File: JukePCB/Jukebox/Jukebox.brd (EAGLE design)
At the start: 133.5 x 197 mm, 31 parts, among them CN1 1X4-BIG

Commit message: board proto 1
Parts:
- moved A2 12.0 mm to (-15.0, 14.0)
- moved N1 12.0 mm to (-15.0, 26.0)
- moved CONTROL1 6.00 mm to (-30.7, -26.0)
- moved CN1 2.00 mm to (-38.3, 48.0)
- moved CONTROL2 1.00 mm to (-30.7, -29.0)
- moved J2 0.70 mm to (-35.8, 54.0)
- turned AUXIN to 90 degrees
- turned AUXOUT to 90 degrees
- turned FROMNEEDLE to 90 degrees
- turned TOAMP to 90 degrees
- turned TOLIGHT to 90 degrees
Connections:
- net GND: now also U$1.GND1
- net N$31: now also U$1.A7; no longer U$1.A3
- net N$32: now also J4.1
- net N$36: now also U$1.A3; no longer U$1.A7
- net N$8: no longer J4.1
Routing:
- net GND: track 0.00 -> 447.8 mm, vias 0 -> 8
- net N$4: track 0.00 -> 402.2 mm, vias 0 -> 2
- net N$3: track 0.00 -> 383.3 mm, vias 0 -> 4
- net N$2: track 0.00 -> 364.3 mm, vias 0 -> 4
- net N$1: track 0.00 -> 358.2 mm, vias 0 -> 4
- net N$10: track 0.00 -> 355.0 mm, vias 0 -> 2
- net N$11: track 0.00 -> 274.1 mm
- net N$27: track 0.00 -> 214.7 mm, vias 0 -> 4
- net N$32: track 0.00 -> 199.8 mm, vias 0 -> 2
- net N$8: track 0.00 -> 150.3 mm
- net N$5: track 0.00 -> 144.5 mm
- net N$6: track 0.00 -> 138.8 mm
- net N$7: track 0.00 -> 133.1 mm
- net N$22: track 0.00 -> 129.1 mm, vias 0 -> 4
- net N$37: track 0.00 -> 126.8 mm, vias 0 -> 2
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
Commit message: almost final routes
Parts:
- A1, A2, N1, N2: value 10k -> 1k
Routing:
- net GND: track 447.8 -> 113.8 mm, vias 8 -> 0
- net N$34: track 118.2 -> 120.8 mm
- net N$25: track 126.3 -> 128.1 mm
- net N$37: track 126.8 -> 128.2 mm
- net N$22: track 129.1 -> 130.2 mm
- added copper zone on layer 16, net GND

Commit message: Anime.mp4
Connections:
- net GND: now also U$8.12; no longer U$8.1
- net N$8: now also U$8.10; no longer U$8.3
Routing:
- net GND: track 113.8 -> 0.00 mm
- net N$8: track 150.3 -> 121.0 mm
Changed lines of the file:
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@@
 </signal>
 <signal name="N$8">
-<contactref element="U$8" pad="3"/>
 <contactref element="U$14" pad="3"/>
-<wire x1="29" y1="-86" x2="34.5" y2="-86" width="1.4224" layer="16"/>
-<wire x1="34.5" y1="-86" x2="34.5" y2="-96.5" width="1.4224" layer="16"/>
-<wire x1="34.5" y1="-96.5" x2="65" y2="-96.5" width="1.4224" layer="16"/>
-<wire x1="65" y1="-96.5" x2="65" y2="2.5" width="1.4224" layer="16"/>
-<wire x1="65" y1="2.5" x2="60.25" y2="2.25" width="1.4224" layer="16"/>
+<contactref element="U$8" pad="10"/>
+<wire x1="29" y1="-86" x2="34.75" y2="-86" width="1.4224" layer="16"/>
+<wire x1="34.75" y1="-86" x2="34.75" y2="-95.75" width="1.4224" layer="16"/>
+<wire x1="34.75" y1="-95.75" x2="65.25" y2="-95.75" width="1.4224" layer="16"/>
+<wire x1="65.25" y1="-95.75" x2="65.25" y2="-26" width="1.4224" layer="16"/>
+<wire x1="65.25" y1="-26" x2="60.25" y2="-26" width="1.4224" layer="16"/>
+<wire x1="60.25" y1="-26" x2="60.25" y2="-25.75" width="1.4224" layer="16"/>
 </signal>
 <signal name="N$33">
@@
 <contactref element="TOLIGHT" pad="1"/>
 <contactref element="U$7" pad="6"/>
-<contactref element="U$8" pad="1"/>
 <contactref element="J3" pad="1"/>
 <contactref element="U$13" pad="1"/>
@@
 <contactref element="U$1" pad="GND"/>
 <contactref element="CONTROL2" pad="1"/>
-<wire x1="-37" y1="-10" x2="-37" y2="2" width="0.4064" layer="16"/>
-<wire x1="-37" y1="2" x2="-37" y2="14" width="0.4064" layer="16"/>
-<wire x1="-37" y1="14" x2="-37" y2="26" width="0.4064" layer="16"/>
-<wire x1="-37" y1="26" x2="-37" y2="38" width="0.4064" layer="16"/>
 <contactref element="U$1" pad="GND1"/>
-<wire x1="5" y1="92" x2="32.5" y2="92" width="0.4064" layer="16"/>
-<wire x1="32.5" y1="92" x2="57.5" y2="67" width="0.4064" layer="16"/>
-<wire x1="57.5" y1="67" x2="59.75" y2="67" width="0.4064" layer="16"/>
-<wire x1="59.75" y1="67" x2="60.25" y2="66.5" width="0.4064" layer="16"/>
 <polygon width="0.4064" layer="16" isolate="0.4064">
 <vertex x="-66.75" y="98.5"/>
@@
 <vertex x="-66.75" y="-98.5"/>
 </polygon>
+<contactref element="U$8" pad="12"/>
 </signal>
 <signal name="N$22">

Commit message: Various desgin tweaks (see commit message)
1.Re routed some traces to eliminate some jumpers.
2. Ran ratsnest to fill in ground plane
Note: I ran a DRC and it gave me a bunch of stop errors. This is becouse compontent silkscreens were confilcting with their pads. As we're not using a silk screen this should be fine
Note: In the upper left hand side there's a jumper that looks like it goes no where. This is connedcting the ground plane of the audio jack to the rest of the board as it got enclosed.
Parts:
- moved N2 7.79 mm to (-20.2, 7.75), turned to 90 degrees
- moved A2 7.36 mm to (-16.2, 21.2), turned to 180 degrees
- moved N1 2.57 mm to (-16.2, 28.2)
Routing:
- net N$13: track 61.6 -> 83.3 mm, vias 2 -> 0
- net N$14: track 67.6 -> 86.0 mm, vias 2 -> 0
- net N$23: track 58.0 -> 40.7 mm, vias 1 -> 0
- net GND: track 0.00 -> 15.3 mm, vias 0 -> 2
- net N$22: track 130.2 -> 125.9 mm, vias 4 -> 2
- net N$24: track 56.3 -> 52.7 mm, vias 2 -> 0
- net N$17: track 36.7 -> 38.8 mm
- net N$16: track 16.7 -> 14.9 mm
- net N$25: track 128.1 -> 126.4 mm, vias 4 -> 2
- net N$19: vias 2 -> 0
- net N$27: vias 4 -> 2

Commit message: Update.exe
I changed the ground trace so that the gound plane is intact and made
the traces a little better
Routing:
- net GND: track 15.3 -> 0.00 mm, vias 2 -> 0
- net N$19: track 90.6 -> 78.1 mm, vias 0 -> 2
- net N$13: track 83.3 -> 71.8 mm
- net N$22: track 125.9 -> 119.1 mm
- net N$24: track 52.7 -> 47.0 mm
- net N$25: track 126.4 -> 120.8 mm
- net N$14: track 86.0 -> 81.9 mm
- net N$23: track 40.7 -> 39.4 mm
- net N$16: track 14.9 -> 16.1 mm
- net N$17: track 38.8 -> 39.6 mm
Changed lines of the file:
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@@
 <contactref element="FROMNEEDLE" pad="3"/>
 <contactref element="N2" pad="P$1"/>
-<wire x1="-34.5" y1="-0.5" x2="-20.25" y2="3.94" width="0.4064" layer="16"/>
+<wire x1="-20.25" y1="3.94" x2="-30.06" y2="3.94" width="0.4064" layer="16"/>
+<wire x1="-30.06" y1="3.94" x2="-34.5" y2="-0.5" width="0.4064" layer="16"/>
 </signal>
 <signal name="N$17">
 <contactref element="FROMNEEDLE" pad="2"/>
 <contactref element="N1" pad="P$1"/>
-<wire x1="-34.5" y1="4.5" x2="-17.5" y2="8" width="0.4064" layer="16"/>
-<wire x1="-17.5" y1="8" x2="-15.5" y2="24.19" width="0.4064" layer="16"/>
-<wire x1="-15.5" y1="24.19" x2="-12.44" y2="28.25" width="0.4064" layer="16"/>
+<wire x1="-34.5" y1="4.5" x2="-31.75" y2="7.25" width="0.4064" layer="16"/>
+<wire x1="-31.75" y1="7.25" x2="-20.25" y2="7.25" width="0.4064" layer="16"/>
+<wire x1="-20.25" y1="7.25" x2="-17.25" y2="10.25" width="0.4064" layer="16"/>
+<wire x1="-17.25" y1="10.25" x2="-17.25" y2="23.44" width="0.4064" layer="16"/>
+<wire x1="-17.25" y1="23.44" x2="-12.44" y2="28.25" width="0.4064" layer="16"/>
 </signal>
 <signal name="N$18">
@@
 <contactref element="A2" pad="P$1"/>
 <contactref element="CN1" pad="1"/>
-<wire x1="-12.44" y1="21.25" x2="-5.31" y2="19.94" width="0.4064" layer="16"/>
-<wire x1="-5.31" y1="19.94" x2="-5.5" y2="28" width="0.4064" layer="16"/>
-<wire x1="-5.5" y1="28" x2="-5.5" y2="36" width="0.4064" layer="16"/>
 <wire x1="-5.5" y1="36" x2="-11" y2="41.5" width="0.4064" layer="16"/>
 <wire x1="-11" y1="41.5" x2="-18" y2="41.5" width="0.4064" layer="16"/>
@@
 <wire x1="-28.5" y1="52" x2="-34.3" y2="52" width="0.4064" layer="16"/>
 <wire x1="-34.3" y1="52" x2="-38.3" y2="48" width="0.4064" layer="16"/>
-<wire x1="-41.5" y1="33.75" x2="-41.5" y2="48" width="0.4064" layer="16"/>
-<wire x1="-41.5" y1="48" x2="-38.3" y2="48" width="0.4064" layer="16"/>
-<wire x1="-41.5" y1="33.75" x2="-34.5" y2="33.75" width="0.4064" layer="16"/>
-<wire x1="-34.5" y1="33.75" x2="-34.5" y2="35.5" width="0.4064" layer="16"/>
+<wire x1="-5.5" y1="36" x2="-5.5" y2="28.19" width="0.4064" layer="16"/>
+<wire x1="-5.5" y1="28.19" x2="-12.44" y2="21.25" width="0.4064" layer="16"/>
+<wire x1="-38.3" y1="48" x2="-38.3" y2="44.55" width="0.4064" layer="16"/>
+<wire x1="-38.3" y1="44.55" x2="-37.5" y2="43.75" width="0.4064" layer="16"/>
+<wire x1="-37.5" y1="43.75" x2="-33.75" y2="43.75" width="0.4064" layer="1"/>
+<wire x1="-33.75" y1="43.75" x2="-30.75" y2="40.75" width="0.4064" layer="16"/>
+<wire x1="-30.75" y1="40.75" x2="-30.75" y2="39.25" width="0.4064" layer="16"/>
+<wire x1="-30.75" y1="39.25" x2="-34.5" y2="35.5" width="0.4064" layer="16"/>
+<via x="-37.5" y="43.75" extent="1-16" drill="0.6" shape="square"/>
+<via x="-33.75" y="43.75" extent="1-16" drill="0.6" shape="square"/>
 </signal>
 <signal name="N$23">
@@
 <contactref element="AUXOUT" pad="3"/>
 <contactref element="TOLIGHT" pad="3"/>
-<wire x1="-34.5" y1="11.5" x2="-27.75" y2="11.5" width="0.4064" layer="16"/>
-<wire x1="-27.75" y1="11.5" x2="-20.25" y2="11.56" width="0.4064" layer="16"/>
-<wire x1="-20.06" y1="21.25" x2="-27.75" y2="21.25" width="0.4064" layer="16"/>
-<wire x1="-27.75" y1="21.25" x2="-27.75" y2="11.5" width="0.4064" layer="16"/>
-<wire x1="-27.75" y1="21.25" x2="-27.75" y2="23.5" width="0.4064" layer="16"/>
-<wire x1="-27.75" y1="23.5" x2="-34.5" y2="23.5" width="0.4064" layer="16"/>
+<wire x1="-34.5" y1="23.5" x2="-22.31" y2="23.5" width="0.4064" layer="16"/>
+<wire x1="-22.31" y1="23.5" x2="-20.06" y2="21.25" width="0.4064" layer="16"/>
+<wire x1="-20.06" y1="21.25" x2="-20.06" y2="11.75" width="0.4064" layer="16"/>
+<wire x1="-20.06" y1="11.75" x2="-20.25" y2="11.56" width="0.4064" layer="16"/>
+<wire x1="-34.5" y1="11.5" x2="-20.31" y2="11.5" width="0.4064" layer="16"/>
+<wire x1="-20.31" y1="11.5" x2="-20.25" y2="11.56" width="0.4064" layer="16"/>
 </signal>
 <signal name="N$24">
@@
 <contactref element="AUXOUT" pad="2"/>
 <contactref element="TOLIGHT" pad="2"/>
-<wire x1="-11.19" y1="38" x2="-11.19" y2="33.62" width="0.4064" layer="16"/>
-<wire x1="-11.19" y1="33.62" x2="-20.06" y2="28.25" width="0.4064" layer="16"/>
 <wire x1="-34.5" y1="28.5" x2="-21.31" y2="28.5" width="0.4064" layer="16"/>
 <wire x1="-21.31" y1="28.5" x2="-20.06" y2="28.25" width="0.4064" layer="16"/>
-<wire x1="-34.5" y1="28.5" x2="-40.25" y2="28.5" width="0.4064" layer="16"/>
-<wire x1="-40.25" y1="28.5" x2="-40.25" y2="16.5" width="0.4064" layer="16"/>
-<wire x1="-40.25" y1="16.5" x2="-34.5" y2="16.5" width="0.4064" layer="16"/>
+<wire x1="-11.19" y1="38" x2="-11.19" y2="37.12" width="0.4064" layer="16"/>
+<wire x1="-11.19" y1="37.12" x2="-20.06" y2="28.25" width="0.4064" layer="16"/>
+<wire x1="-34.5" y1="28.5" x2="-38.5" y2="28.5" width="0.4064" layer="16"/>
+<wire x1="-38.5" y1="28.5" x2="-40.25" y2="26.75" width="0.4064" layer="16"/>
+<wire x1="-40.25" y1="26.75" x2="-40.25" y2="22.25" width="0.4064" layer="16"/>
+<wire x1="-40.25" y1="22.25" x2="-34.5" y2="16.5" width="0.4064" layer="16"/>
 </signal>
 <signal name="N$27">
@@
 </polygon>
 <contactref element="U$8" pad="12"/>
-<wire x1="-37" y1="38" x2="-38.75" y2="42.5" width="0.4064" layer="16"/>
-<wire x1="-38.75" y1="42.5" x2="-46.75" y2="42.5" width="0.4064" layer="1"/>
-<wire x1="-46.75" y1="42.5" x2="-48.25" y2="40.5" width="0.4064" layer="16"/>
-<via x="-38.75" y="42.5" extent="1-16" drill="0.6" shape="square"/>
-<via x="-46.75" y="42.5" extent="1-16" drill="0.6" shape="square"/>
 </signal>
 <signal name="N$22">
@@
 <wire x1="58.25" y1="-66.25" x2="51" y2="-59" width="0.4064" layer="16"/>
 <wire x1="51" y1="-59" x2="51" y2="-57" width="0.4064" layer="16"/>
-<wire x1="51" y1="22" x2="51" y2="33.75" width="0.4064" layer="16"/>
-<wire x1="30.08" y1="33.81" x2="51" y2="33.75" width="0.4064" layer="16"/>
+<wire x1="30.08" y1="33.81" x2="39.19" y2="33.81" width="0.4064" layer="16"/>
+<wire x1="39.19" y1="33.81" x2="51" y2="22" width="0.4064" layer="16"/>
 </signal>
 <signal name="N$25">
 <contactref element="U$17" pad="4"/>
 <contactref element="U$1" pad="D2"/>
-<wire x1="30.08" y1="31.27" x2="30.27" y2="31.27" width="0.4064" layer="16"/>
 <wire x1="48" y1="22" x2="48" y2="-58" width="0.4064" layer="1"/>
 <via x="48" y="22" extent="1-16" drill="0.6" shape="square"/>
@@
 <wire x1="57.25" y1="-70.25" x2="48" y2="-61" width="0.4064" layer="16"/>
 <wire x1="48" y1="-61" x2="48" y2="-58" width="0.4064" layer="16"/>
-<wire x1="48" y1="22" x2="48" y2="31.25" width="0.4064" layer="16"/>
-<wire x1="48" y1="31.25" x2="30.1" y2="31.25" width="0.4064" layer="16"/>
-<wire x1="30.1" y1="31.25" x2="30.08" y2="31.27" width="0.4064" layer="16"/>
+<wire x1="30.1" y1="31.25" x2="38.75" y2="31.25" width="0.4064" layer="16"/>
+<wire x1="38.75" y1="31.25" x2="48" y2="22" width="0.4064" layer="16"/>
+<wire x1="30.1" y1="31.25" x2="30.08" y2="31.27" width="0" layer="19" extent="16-16"/>
 </signal>
 <signal name="N$34">
@@
 <contactref element="CN1" pad="3"/>
 <contactref element="TOAMP" pad="2"/>
-<wire x1="-33.22" y1="48" x2="-32" y2="46.78" width="0.4064" layer="16"/>
-<wire x1="-32" y1="46.78" x2="-32" y2="32.25" width="0.4064" layer="16"/>
-<wire x1="-32" y1="32.25" x2="-47" y2="32.25" width="0.4064" layer="16"/>
-<wire x1="-47" y1="32.25" x2="-46.75" y2="-7.5" width="0.4064" layer="16"/>
-<wire x1="-46.75" y1="-7.5" x2="-34.5" y2="-7.5" width="0.4064" layer="16"/>
+<wire x1="-33.22" y1="48" x2="-33.22" y2="44.72" width="0.4064" layer="16"/>
+<wire x1="-33.22" y1="44.72" x2="-29.25" y2="40.75" width="0.4064" layer="16"/>
+<wire x1="-29.25" y1="40.75" x2="-29.25" y2="34" width="0.4064" layer="16"/>
+<wire x1="-29.25" y1="34" x2="-30.5" y2="32.75" width="0.4064" layer="16"/>
+<wire x1="-30.5" y1="32.75" x2="-38.75" y2="32.75" width="0.4064" layer="16"/>
+<wire x1="-38.75" y1="32.75" x2="-43.75" y2="27.75" width="0.4064" layer="16"/>
+<wire x1="-43.75" y1="27.75" x2="-43.75" y2="1.75" width="0.4064" layer="16"/>
+<wire x1="-43.75" y1="1.75" x2="-34.5" y2="-7.5" width="0.4064" layer="16"/>
 </signal>
 <signal name="N$14">
 <contactref element="TOAMP" pad="3"/>
 <contactref element="CN1" pad="4"/>
-<wire x1="-30.68" y1="48" x2="-30.68" y2="30.82" width="0.4064" layer="16"/>
-<wire x1="-30.68" y1="30.82" x2="-30.75" y2="30.75" width="0.4064" layer="16"/>
-<wire x1="-30.75" y1="30.75" x2="-42.25" y2="30.75" width="0.4064" layer="16"/>
-<wire x1="-42.25" y1="30.75" x2="-42" y2="-4.25" width="0.4064" layer="16"/>
-<wire x1="-42" y1="-4.25" x2="-31.25" y2="-4.25" width="0.4064" layer="16"/>
-<wire x1="-31.25" y1="-4.25" x2="-31.25" y2="-12.5" width="0.4064" layer="16"/>
-<wire x1="-31.25" y1="-12.5" x2="-34.5" y2="-12.5" width="0.4064" layer="16"/>
+<wire x1="-30.68" y1="48" x2="-30.68" y2="43.68" width="0.4064" layer="16"/>
+<wire x1="-30.68" y1="43.68" x2="-27.75" y2="40.75" width="0.4064" layer="16"/>
+<wire x1="-27.75" y1="40.75" x2="-27.75" y2="33.25" width="0.4064" layer="16"/>
+<wire x1="-27.75" y1="33.25" x2="-29.5" y2="31.5" width="0.4064" layer="16"/>
+<wire x1="-29.5" y1="31.5" x2="-38.5" y2="31.5" width="0.4064" layer="16"/>
+<wire x1="-38.5" y1="31.5" x2="-42.25" y2="27.75" width="0.4064" layer="16"/>
+<wire x1="-42.25" y1="27.75" x2="-42.25" y2="3.25" width="0.4064" layer="16"/>
+<wire x1="-42.25" y1="3.25" x2="-34.5" y2="-4.5" width="0.4064" layer="16"/>
+<wire x1="-34.5" y1="-4.5" x2="-33" y2="-4.5" width="0.4064" layer="16"/>
+<wire x1="-34.5" y1="-12.5" x2="-33" y2="-12.5" width="0.4064" layer="16"/>
+<wire x1="-33" y1="-12.5" x2="-29.75" y2="-9.25" width="0.4064" layer="16"/>
+<wire x1="-29.75" y1="-9.25" x2="-29.75" y2="-7.75" width="0.4064" layer="16"/>
+<wire x1="-29.75" y1="-7.75" x2="-33" y2="-4.5" width="0.4064" layer="16"/>
 </signal>
 <signal name="N$15">

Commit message: Board Update, Not Final
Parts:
- moved TOAMP 36.0 mm to (-34.5, 26.0)
- moved AUXOUT 12.0 mm to (-34.5, 14.0)
- moved FROMNEEDLE 12.0 mm to (-34.5, -10.0)
- moved TOLIGHT 12.0 mm to (-34.5, 2.00)
- moved N2 7.63 mm to (-16.2, 14.2), turned to 180 degrees
- moved A1 3.02 mm to (-16.2, 35.2)
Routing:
- net N$14: track 81.9 -> 30.4 mm
- net N$13: track 71.8 -> 24.4 mm
- net N$16: track 16.1 -> 38.1 mm
- net N$10: track 355.0 -> 376.4 mm, vias 2 -> 0
- net N$24: track 47.0 -> 64.5 mm
- net N$17: track 39.6 -> 46.1 mm
- net N$19: track 78.1 -> 82.8 mm, vias 2 -> 0
- net N$18: track 32.7 -> 36.8 mm
- net N$4: track 402.2 -> 398.9 mm
- net N$9: track 120.1 -> 119.4 mm

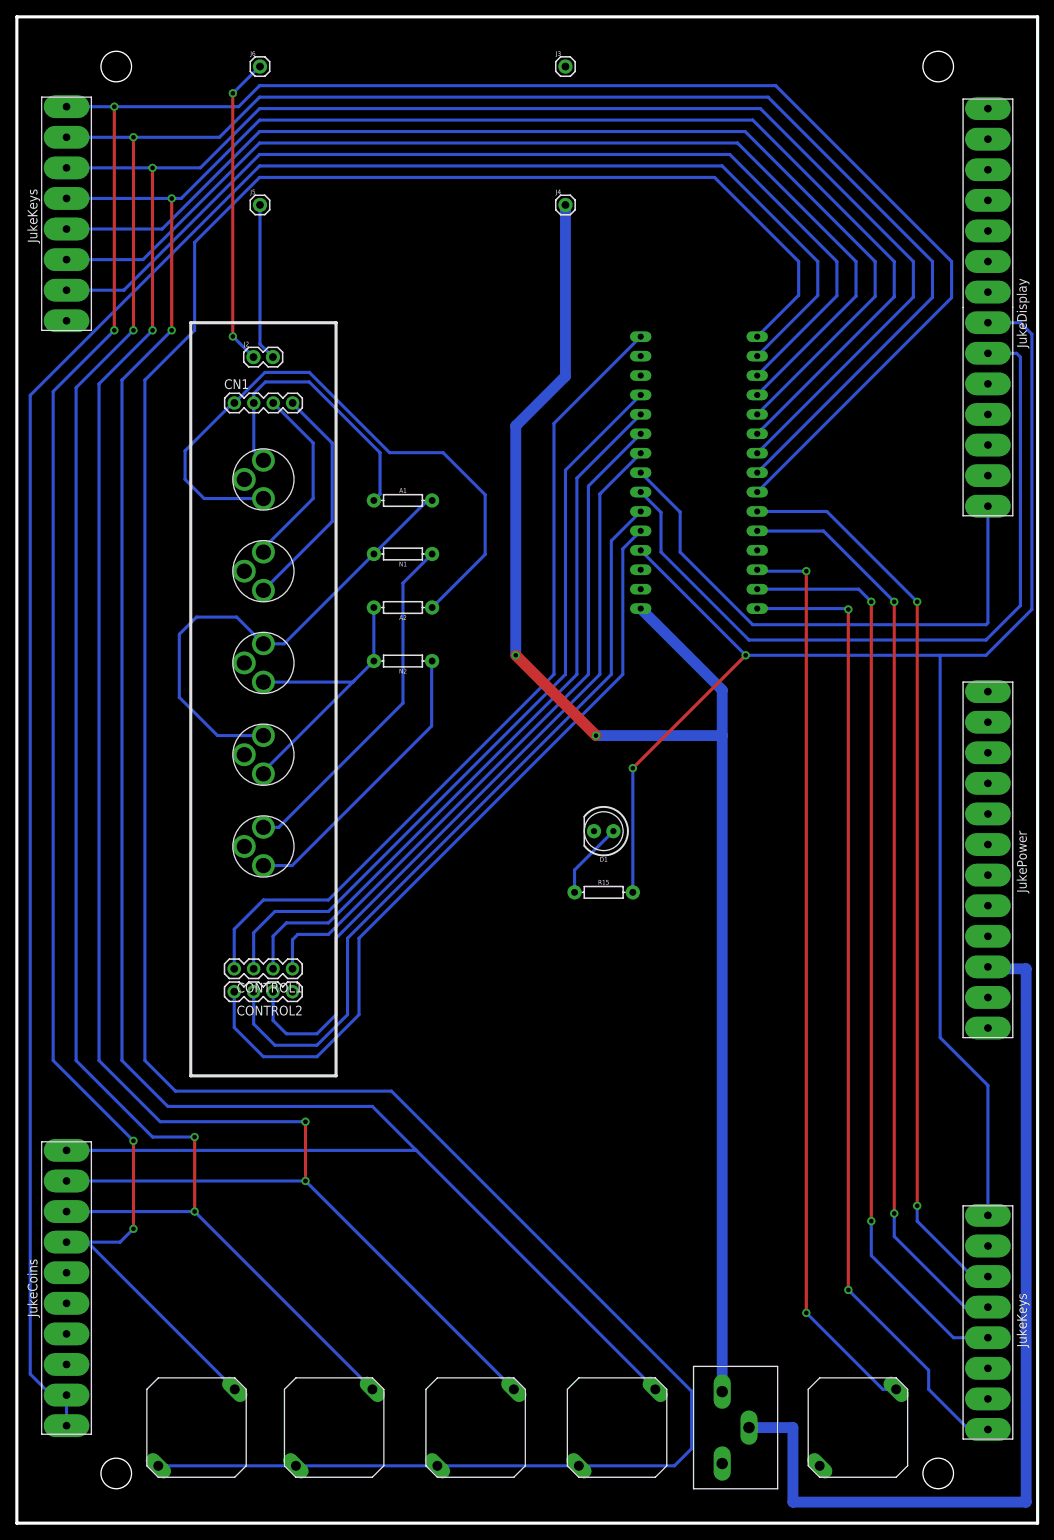
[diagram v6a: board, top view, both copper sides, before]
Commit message: Added not ground plane fixed some traces, need to fix audio bits
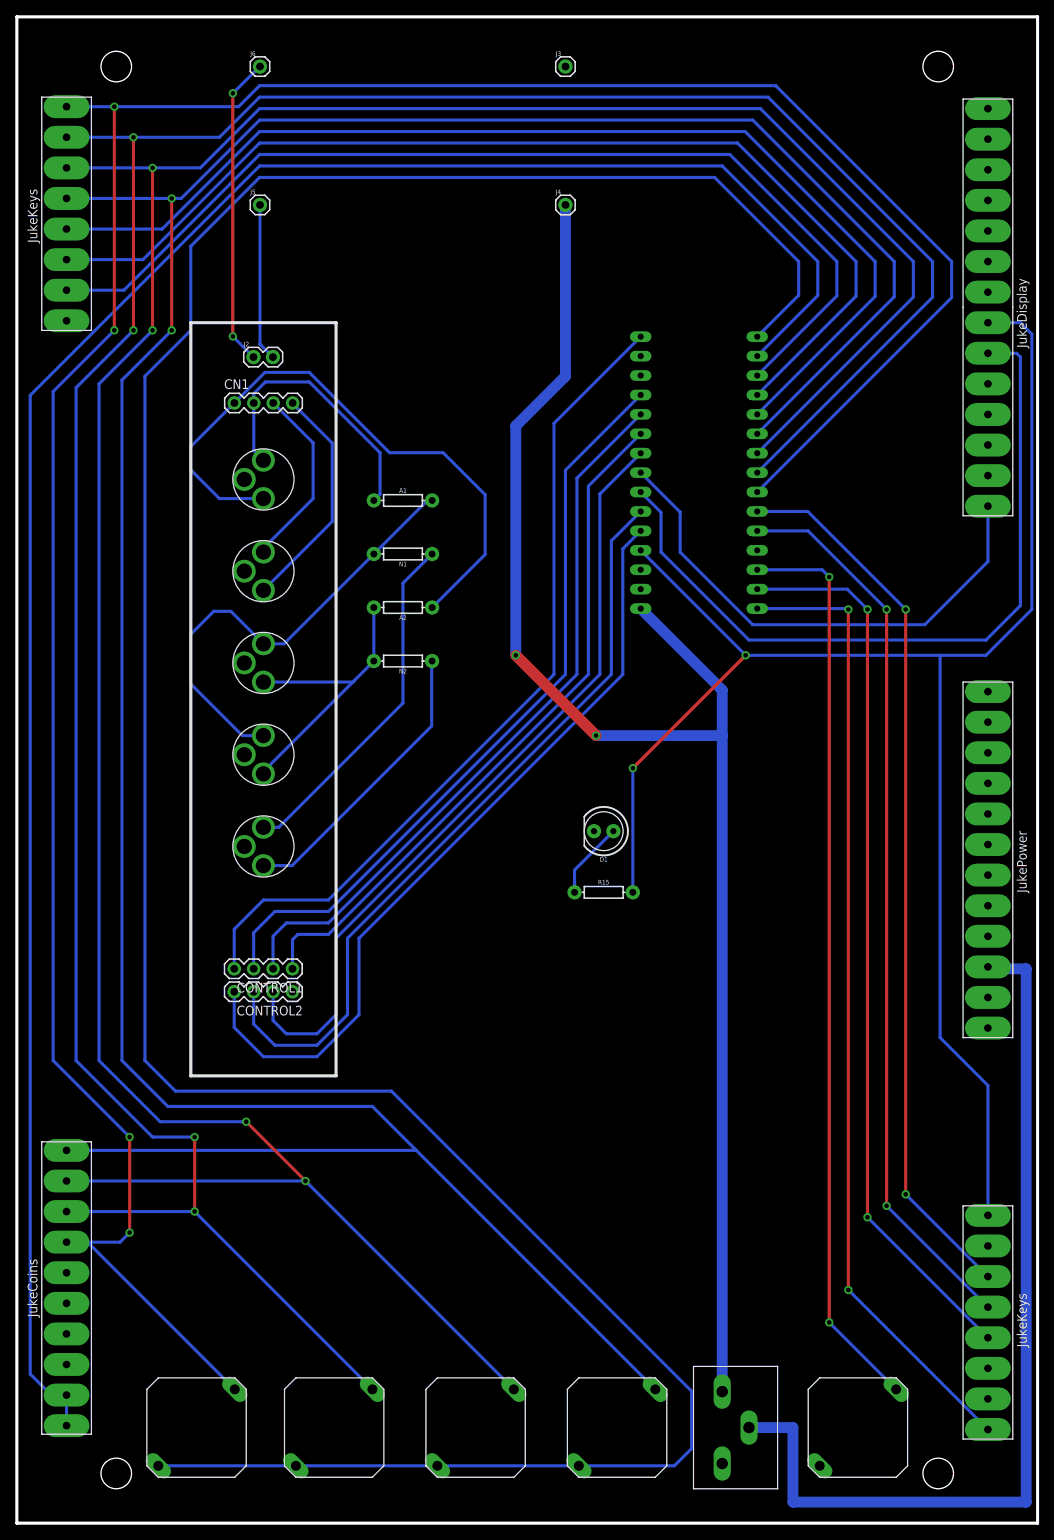
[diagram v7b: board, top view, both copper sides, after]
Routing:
- net N$12: track 72.1 -> 67.4 mm
- net N$3: track 383.3 -> 378.7 mm
- net N$34: track 120.8 -> 117.3 mm
- net N$24: track 64.5 -> 61.1 mm
- net N$25: track 120.8 -> 117.9 mm
- net N$22: track 119.1 -> 116.4 mm
- net N$1: track 358.2 -> 360.5 mm
- net N$19: track 82.8 -> 81.1 mm
- net N$37: track 128.2 -> 126.8 mm
- added copper zone on layer 16, net NOTGROUND
